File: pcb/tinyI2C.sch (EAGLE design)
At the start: 38 parts, among them IC1 74LVC1G125DCK, IC2 74LVC1G125DCK, IC3 IC_LDO_MIC5355, Q1 12MHz, U1 LPC824M201JHI33, X1 TSW-112-02-S-S, X2 TSW-112-02-S-S, X3 TSW-106-02-S-S-RA, X4 TSW-102-02-S-S, X5 TSW-102-02-S-S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

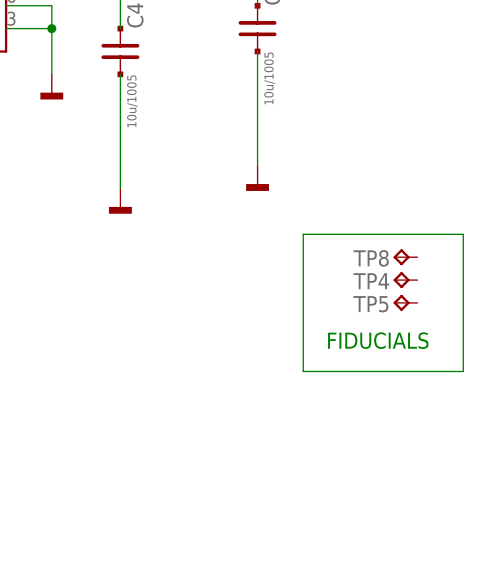
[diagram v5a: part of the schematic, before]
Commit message: [ PCB ][ SCH ] FIDUCIAL from library
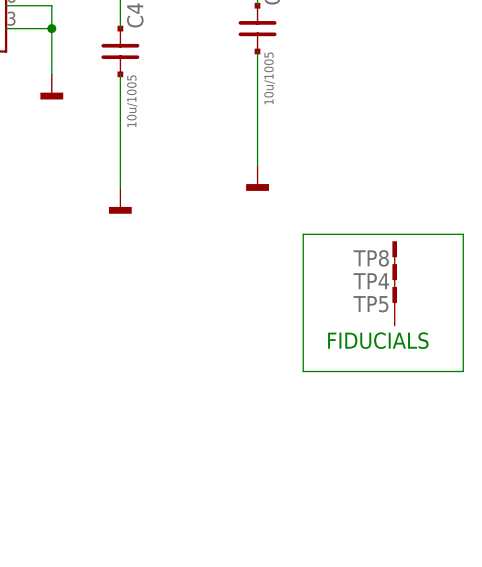
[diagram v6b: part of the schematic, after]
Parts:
- TP4, TP5, TP8: value TPTP20R -> TESTPAD_F; device testpad_local:TPTP20R -> mylib:TESTPAD_F
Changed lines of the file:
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@@
 <part name="X4" library="con-samtec.local" deviceset="TSW-102-02-S-S" device=""/>
 <part name="GND12" library="mbed-HDK" deviceset="GND" device=""/>
-<part name="TP4" library="testpad_local" deviceset="TP" device="TP20R" value="TPTP20R"/>
-<part name="TP5" library="testpad_local" deviceset="TP" device="TP20R" value="TPTP20R"/>
+<part name="TP4" library="mylib" deviceset="TESTPAD" device="_F" value="TESTPAD_F"/>
+<part name="TP5" library="mylib" deviceset="TESTPAD" device="_F" value="TESTPAD_F"/>
 <part name="X5" library="con-samtec.local" deviceset="TSW-102-02-S-S" device=""/>
 <part name="X6" library="con-samtec.local" deviceset="TSW-102-02-S-S" device=""/>
@@
 <part name="GND16" library="mbed-HDK" deviceset="GND" device=""/>
 <part name="TP7" library="testpad_local" deviceset="TP" device="B1,27" value="TPB1,27"/>
-<part name="TP8" library="testpad_local" deviceset="TP" device="TP20R" value="TPTP20R"/>
+<part name="TP8" library="mylib" deviceset="TESTPAD" device="_F" value="TESTPAD_F"/>
 <part name="I1" library="mylib" deviceset="ICON_MINLAB" device="_5.2S" value="ICON_MINLAB_5.2S"/>
 <part name="TP2" library="mylib" deviceset="TESTPAD" device=""/>
@@
 </instance>
 <instance part="GND12" gate="1" x="35.56" y="15.24"/>
-<instance part="TP4" gate="G$1" x="246.38" y="35.56" smashed="yes" rot="R90">
+<instance part="TP4" gate="1" x="246.38" y="35.56" smashed="yes" rot="R90">
 <attribute name="NAME" x="245.872" y="34.544" size="1.778" layer="95" rot="MR0"/>
 <attribute name="TP_SIGNAL_NAME" x="247.65" y="36.83" size="1.778" layer="97" rot="R90"/>
 </instance>
-<instance part="TP5" gate="G$1" x="246.38" y="33.02" smashed="yes" rot="R90">
+<instance part="TP5" gate="1" x="246.38" y="33.02" smashed="yes" rot="R90">
 <attribute name="NAME" x="245.872" y="32.004" size="1.778" layer="95" rot="MR0"/>
 <attribute name="TP_SIGNAL_NAME" x="247.65" y="34.29" size="1.778" layer="97" rot="R90"/>
@@
 <attribute name="TP_SIGNAL_NAME" x="161.29" y="49.53" size="1.778" layer="97" rot="R90"/>
 </instance>
-<instance part="TP8" gate="G$1" x="246.38" y="38.1" smashed="yes" rot="R90">
+<instance part="TP8" gate="1" x="246.38" y="38.1" smashed="yes" rot="R90">
 <attribute name="NAME" x="245.872" y="37.084" size="1.778" layer="95" rot="MR0"/>
 <attribute name="TP_SIGNAL_NAME" x="247.65" y="39.37" size="1.778" layer="97" rot="R90"/>

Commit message: update eagle version = 7.5.0; library update
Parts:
- TP3, TP7: value TPB1,27 -> TPTP14R; device testpad_local:TPB1,27 -> testpad_local:TPTP14R
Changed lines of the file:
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@@
 <?xml version="1.0" encoding="utf-8"?>
 <!DOCTYPE eagle SYSTEM "eagle.dtd">
-<eagle version="6.5.0">
+<eagle version="7.5.0">
 <drawing>
 <settings>
@@
 <part name="GND11" library="mbed-HDK" deviceset="GND" device=""/>
 <part name="TP1" library="testpad_local" deviceset="TP" device="TP07R"/>
-<part name="TP3" library="testpad_local" deviceset="TP" device="B1,27" value="TPB1,27"/>
+<part name="TP3" library="testpad_local" deviceset="TP" device="TP14R" value="TPTP14R"/>
 <part name="R1" library="mylib" deviceset="R_US_PAD_PAD" device="_1005" value="220/1005"/>
 <part name="R2" library="mylib" deviceset="R_US_PAD_PAD" device="_1005" value="220/1005"/>
@@
 <part name="C9" library="mylib" deviceset="C_PAD_PAD_" device="1005" value="18p/1005"/>
 <part name="GND16" library="mbed-HDK" deviceset="GND" device=""/>
-<part name="TP7" library="testpad_local" deviceset="TP" device="B1,27" value="TPB1,27"/>
+<part name="TP7" library="testpad_local" deviceset="TP" device="TP14R" value="TPTP14R"/>
 <part name="TP8" library="mylib" deviceset="TESTPAD" device="_F" value="TESTPAD_F"/>
 <part name="I1" library="mylib" deviceset="ICON_MINLAB" device="_5.2S" value="ICON_MINLAB_5.2S"/>

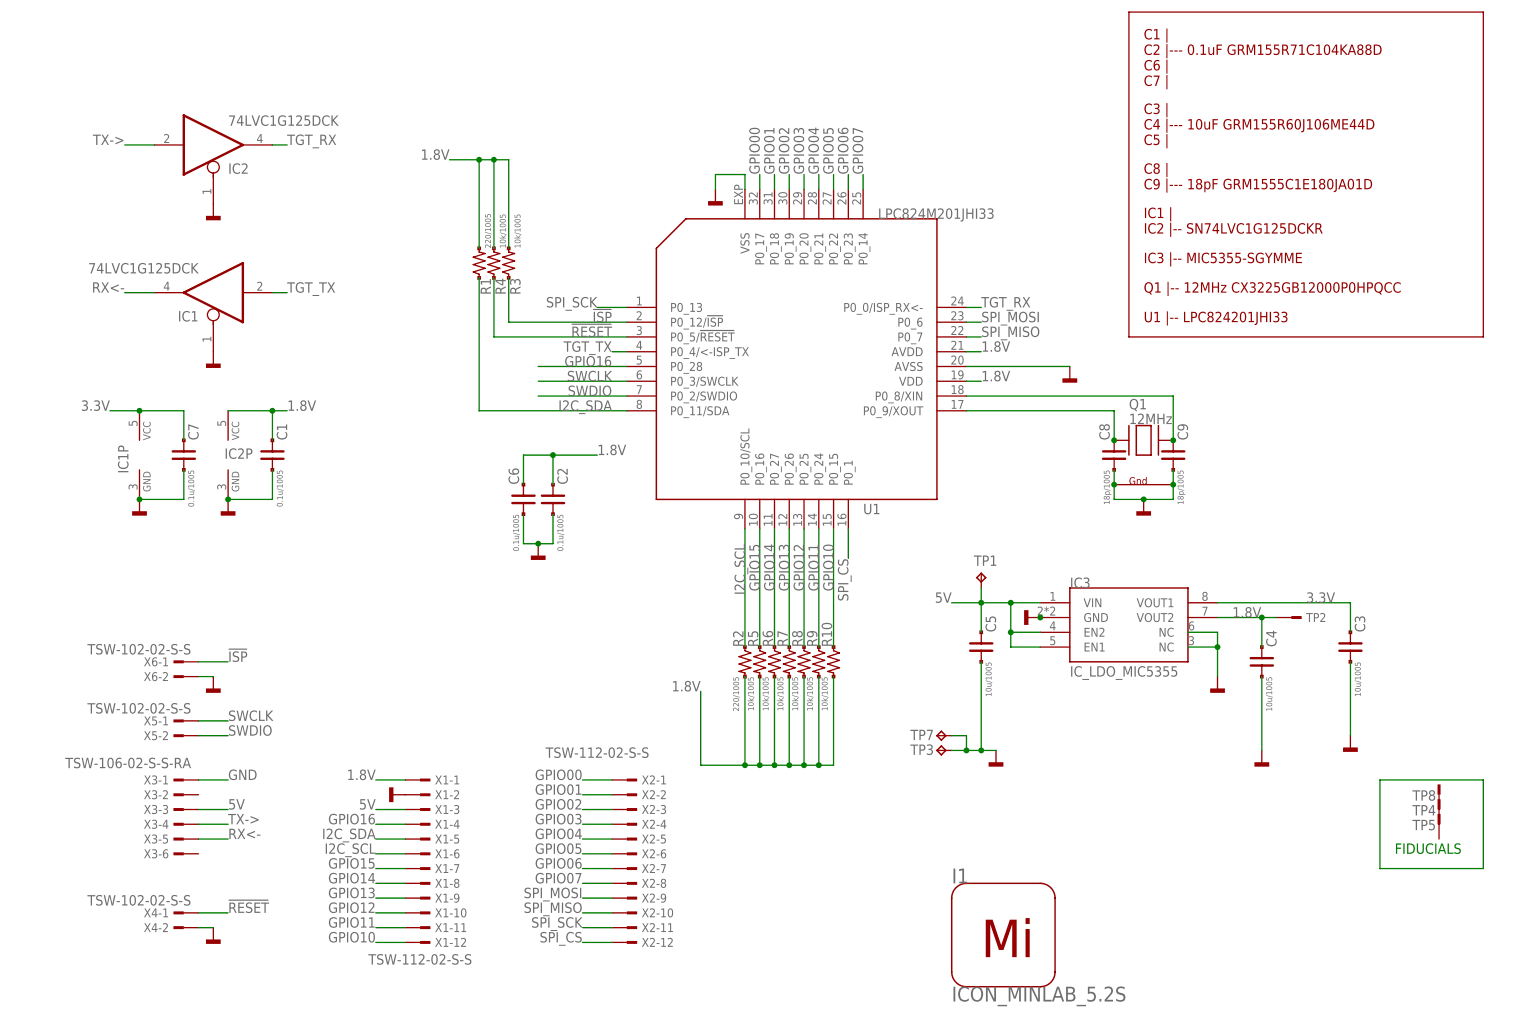
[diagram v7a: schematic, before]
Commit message: [ PCB ] library update
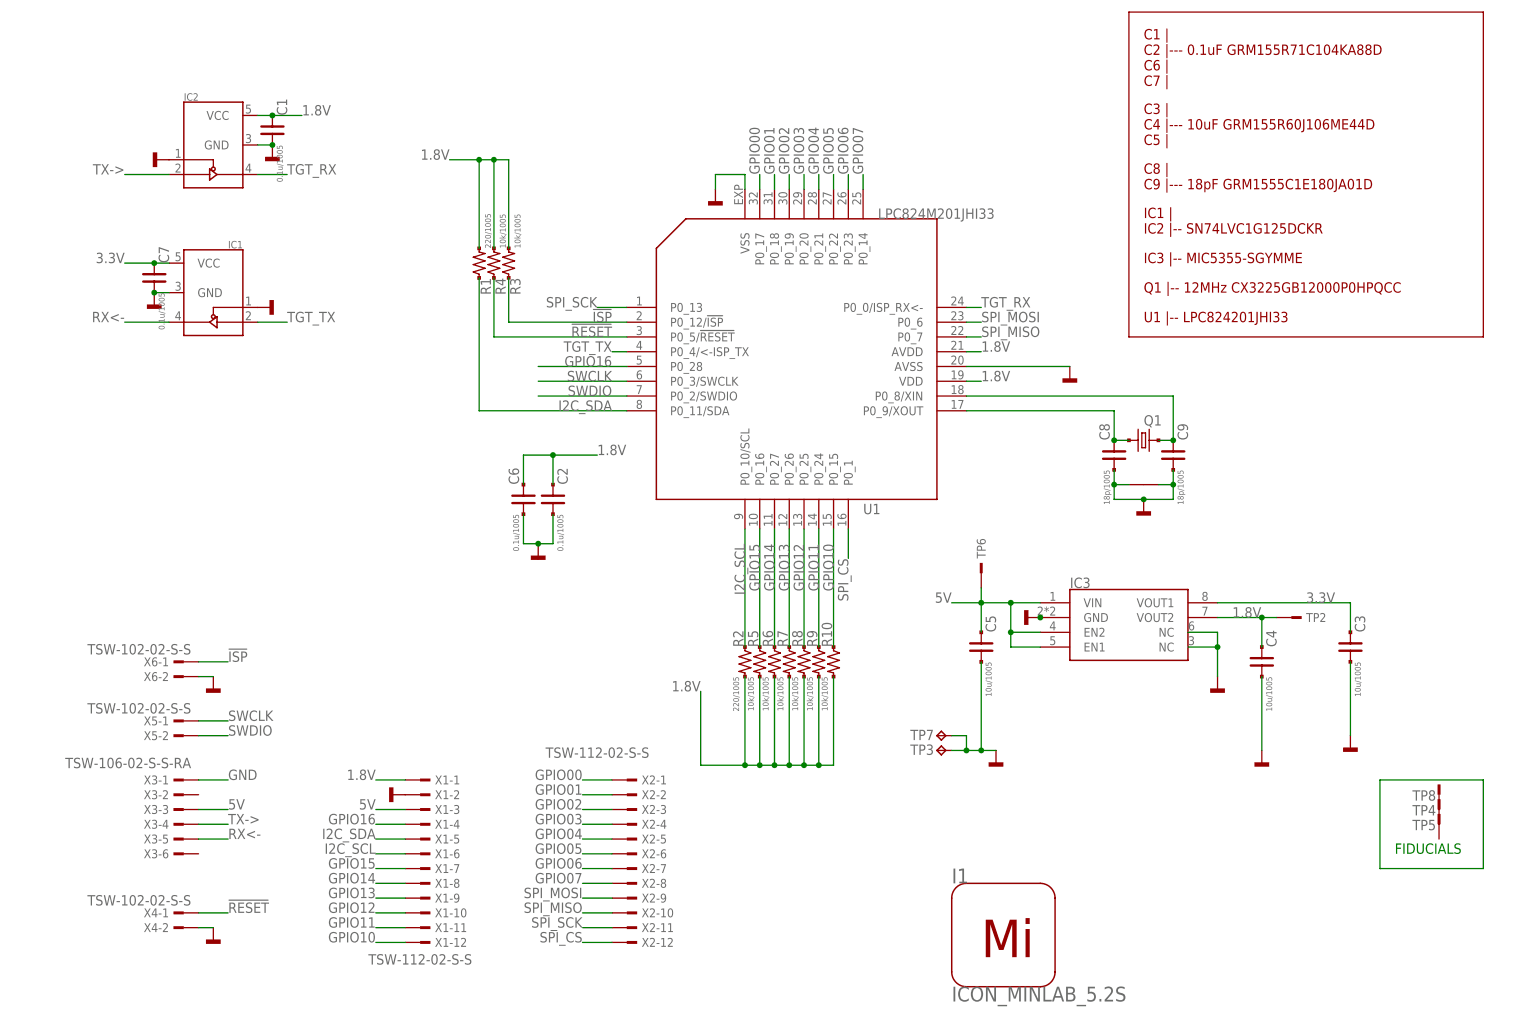
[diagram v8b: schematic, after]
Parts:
- removed TP1: TPTP07R, testpad_local:TPTP07R
- added TP6: TESTPAD, mylib:TESTPAD
- C1, C2, C6, C7: device mylib:C_PAD_PAD_1005 -> mylib:C_SMD_0.1U_1005
- C3, C4, C5: device mylib:C_PAD_PAD_1005 -> mylib:C_SMD_10U_1005
- C8, C9: device mylib:C_PAD_PAD_1005 -> mylib:C_SMD_18P_1005
- IC1, IC2: value 74LVC1G125DCK -> (none); device 74xx-little-us_local:74LVC1G125DCK -> mylib:74LVC1G125_SC70
- IC3: value IC_LDO_MIC5355 -> (none); device mylib:IC_LDO_MIC5355 -> mylib:IC_LDO_MIC5355_3.3/1.8
- Q1: value 12MHz -> (none); device adafruit (1):XTAL-4-3225 -> mylib:CRYSTAL4_12M_3225
- R1, R2: device mylib:R_US_PAD_PAD_1005 -> mylib:R_US_220R_1005
- R10, R3, R4, R5, R6, R7, R8, R9: device mylib:R_US_PAD_PAD_1005 -> mylib:R_US_10K_1005
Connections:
- net 1.8V: now also IC2.VCC; no longer IC2P.VCC
- net 3.3V: now also IC1.VCC; no longer IC1P.VCC
- net 5V: now also TP6.1; no longer TP1.TP
- net GND: now also IC1.!OE!, IC1.GND, IC2.!OE!, IC2.GND, Q1.P$1, Q1.P$2; no longer IC1A.OE, IC1P.GND, IC2A.OE, IC2P.GND, Q1.G1, Q1.G2
- net N$1: now also Q1.1; no longer Q1.X1
- net N$3: now also Q1.2; no longer Q1.X2
- net RX<-: now also IC1.Y; no longer IC1A.O
- net TGT_RX: now also IC2.Y; no longer IC2A.O
- net TGT_TX: now also IC1.A; no longer IC1A.I
- net TX->: now also IC2.A; no longer IC2A.I
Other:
- moved on the sheet: C1, C7
